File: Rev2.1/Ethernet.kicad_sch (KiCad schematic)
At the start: 33 parts, among them J13 8P8C_LED, T1 H1102NLT, U12 USBLC6-4SC6, U8 LAN8742A, Y3 25Mhz

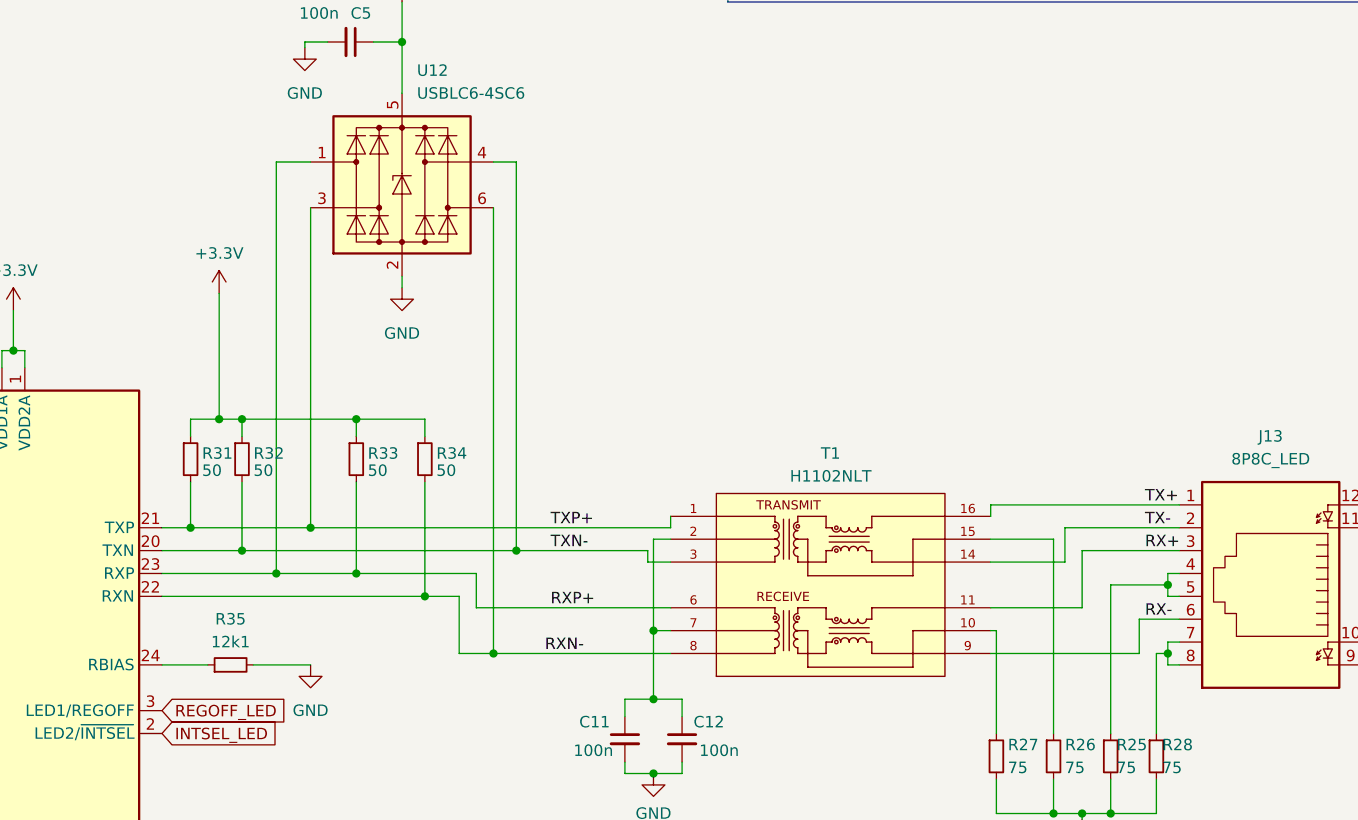
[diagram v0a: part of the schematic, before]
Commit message: added pull up resistors to the I2c Lines for LSM and did mock up placements for PCB
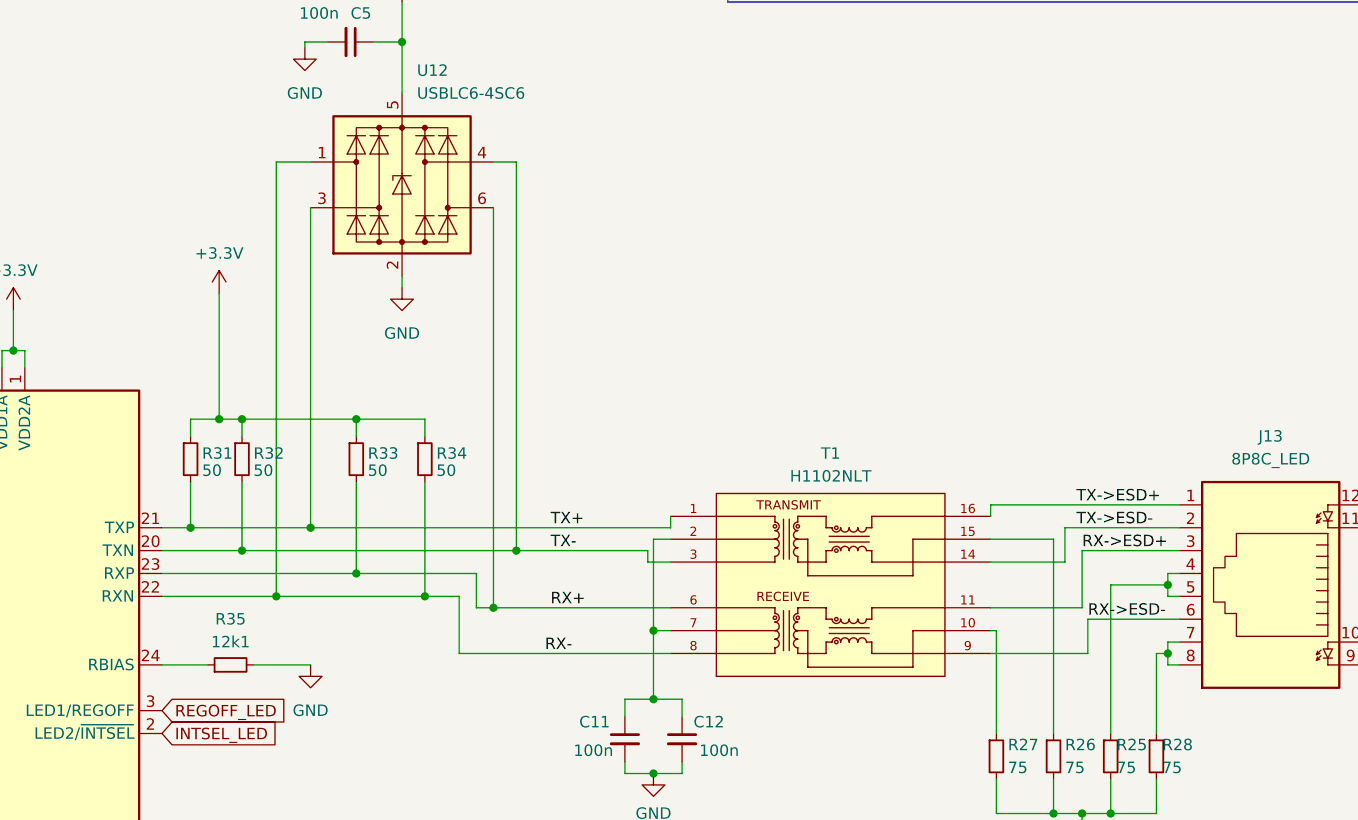
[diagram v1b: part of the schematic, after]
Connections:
- net TXN- is gone; now on net TX-: R32.2, T1.3, U12.4 (I/O3), U8.20 (TXN)
- net TXP+ is gone; now on net TX+: R31.2, T1.1, U12.3 (I/O2), U8.21 (TXP)
- net RX+: now also R33.2, T1.6, U12.6 (I/O4), U8.23 (RXP); no longer J13.3, T1.11
- net RX-: now also R34.2, T1.8, U12.1 (I/O1), U8.22 (RXN); no longer J13.6, T1.9
- net TX+: no longer J13.1, T1.16
- net TX-: no longer J13.2, T1.14
- removed net RXN-: R34.2, T1.8, U12.6 (I/O4), U8.22 (RXN)
- removed net RXP+: R33.2, T1.6, U12.1 (I/O1), U8.23 (RXP)
- new net RX->ESD+: J13.3, T1.11
- new net RX->ESD-: J13.6, T1.9
- new net TX->ESD+: J13.1, T1.16
- new net TX->ESD-: J13.2, T1.14

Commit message: done about 2/3 of the routing for the board
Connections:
- net ETH_RXD1: now also R43.2; no longer R43.1
- net at R40.2, U8.7 (RXD1/MODE1): now also R43.1; no longer R43.2
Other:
- moved on the sheet: R43
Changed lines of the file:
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@@
     )
   )
-  (symbol (lib_id "Device:R_Small") (at 144.78 86.36 0) (unit 1)
-    (in_bom yes) (on_board yes) (dnp no)
-    (property "Reference" "R33" (at 146.05 85.725 0)
-      (effects (font (size 1.27 1.27)) (justify left))
-    )
-    (property "Value" "50" (at 146.05 87.63 0)
+  (symbol (lib_id "Device:R_Small") (at 144.78 86.36 0) (mirror y) (unit 1)
+    (in_bom yes) (on_board yes) (dnp no)
+    (property "Reference" "R33" (at 143.51 85.725 0)
+      (effects (font (size 1.27 1.27)) (justify left))
+    )
+    (property "Value" "50" (at 143.51 87.63 0)
       (effects (font (size 1.27 1.27)) (justify left))
     )
@@
     )
   )
-  (symbol (lib_id "Device:R_Small") (at 68.58 101.6 90) (unit 1)
+  (symbol (lib_id "Device:R_Small") (at 68.58 101.6 270) (mirror x) (unit 1)
     (in_bom yes) (on_board yes) (dnp no)
     (property "Reference" "R43" (at 68.58 103.505 90)

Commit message: finished the first mock up of routing now just need to polish it up
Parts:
- J13: footprint Connector_RJ:RJ45_Wuerth_74980111211_Horizontal -> Connector_RJ:RJ45_Amphenol_RJHSE538X
- R31, R32, R33, R34: footprint Resistor_SMD:R_0603_1608Metric_Pad0.98x0.95mm_HandSolder -> Resistor_SMD:R_0402_1005Metric_Pad0.72x0.64mm_HandSolder
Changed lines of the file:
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@@
       (effects (font (size 1.27 1.27)) (justify left))
     )
-    (property "Footprint" "Resistor_SMD:R_0603_1608Metric_Pad0.98x0.95mm_HandSolder" (at 144.78 86.36 0)
+    (property "Footprint" "Resistor_SMD:R_0402_1005Metric_Pad0.72x0.64mm_HandSolder" (at 144.78 86.36 0)
       (effects (font (size 1.27 1.27)) hide)
     )
@@
       (effects (font (size 1.27 1.27)) (justify left))
     )
-    (property "Footprint" "Resistor_SMD:R_0603_1608Metric_Pad0.98x0.95mm_HandSolder" (at 132.08 86.36 0)
+    (property "Footprint" "Resistor_SMD:R_0402_1005Metric_Pad0.72x0.64mm_HandSolder" (at 132.08 86.36 0)
       (effects (font (size 1.27 1.27)) hide)
     )
@@
       (effects (font (size 1.27 1.27)) (justify left))
     )
-    (property "Footprint" "Resistor_SMD:R_0603_1608Metric_Pad0.98x0.95mm_HandSolder" (at 152.4 86.36 0)
+    (property "Footprint" "Resistor_SMD:R_0402_1005Metric_Pad0.72x0.64mm_HandSolder" (at 152.4 86.36 0)
       (effects (font (size 1.27 1.27)) hide)
     )
@@
       (effects (font (size 1.27 1.27)) (justify left))
     )
-    (property "Footprint" "Resistor_SMD:R_0603_1608Metric_Pad0.98x0.95mm_HandSolder" (at 126.365 86.36 0)
+    (property "Footprint" "Resistor_SMD:R_0402_1005Metric_Pad0.72x0.64mm_HandSolder" (at 126.365 86.36 0)
       (effects (font (size 1.27 1.27)) hide)
     )
@@
       (effects (font (size 1.27 1.27)))
     )
-    (property "Footprint" "Connector_RJ:RJ45_Wuerth_74980111211_Horizontal" (at 246.38 99.695 90)
-      (effects (font (size 1.27 1.27)) hide)
-    )
+    (property "Footprint" "Connector_RJ:RJ45_Amphenol_RJHSE538X" (at 246.38 99.695 90)
+      (effects (font (size 1.27 1.27)) hide)
+    )
